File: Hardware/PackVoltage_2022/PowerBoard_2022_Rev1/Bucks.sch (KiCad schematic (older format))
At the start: 80 parts, among them U10 OKI-78SR-12_1.0-W36-C, U11 OKI-78SR-12_1.0-W36-C, U12 OKI-78SR-12_1.0-W36-C, U13 OKI-78SR-12_1.0-W36-C, U14 OKI-78SR-12_1.0-W36-C, U15 OKI-78SR-12_1.0-W36-C, U16 OKI-78SR-12_1.0-W36-C, U17 OKI-78SR-12_1.0-W36-C, U55 OKI-78SR-12_1.0-W36-C, U7 OKI-78SR-5_1.5-W36-C, U8 OKI-78SR-3.3_1.5-W36-C, U9 OKI-78SR-12_1.0-W36-C

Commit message: Actuation shit
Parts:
- added F9: 5A, Fuse:Fuse_0603_1608Metric_Pad1.05x0.95mm_HandSolder, symbol Device:Fuse
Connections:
- net PV: now also F9.2
- net PVLogic renamed PVAct
- new net PVAct2: F9.1
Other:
- moved on the sheet: F1, F4, F5, F6
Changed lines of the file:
@@
 Wire Wire Line
 	6000 3750 6150 3750
-Text HLabel 750  7000 0    50   Input ~ 0
+Text HLabel 750  6750 0    50   Input ~ 0
 PV
 $Comp
 L Device:Fuse F4
 U 1 1 61DCC65E
-P 1300 6700
-F 0 "F4" V 1103 6700 50  0000 C CNN
-F 1 "5A" V 1194 6700 50  0000 C CNN
-F 2 "Fuse:Fuse_0603_1608Metric_Pad1.05x0.95mm_HandSolder" V 1230 6700 50  0001 C CNN
-F 3 "~" H 1300 6700 50  0001 C CNN
-	1    1300 6700
+P 1300 6450
+F 0 "F4" V 1103 6450 50  0000 C CNN
+F 1 "5A" V 1194 6450 50  0000 C CNN
+F 2 "Fuse:Fuse_0603_1608Metric_Pad1.05x0.95mm_HandSolder" V 1230 6450 50  0001 C CNN
+F 3 "~" H 1300 6450 50  0001 C CNN
+	1    1300 6450
 	0    1    1    0
 $EndComp
@@
 L Device:Fuse F6
 U 1 1 61DCD94F
-P 1300 7300
-F 0 "F6" V 1103 7300 50  0000 C CNN
-F 1 "5A" V 1194 7300 50  0000 C CNN
-F 2 "Fuse:Fuse_0603_1608Metric_Pad1.05x0.95mm_HandSolder" V 1230 7300 50  0001 C CNN
-F 3 "~" H 1300 7300 50  0001 C CNN
-	1    1300 7300
-	0    1    1    0
-$EndComp
-Text GLabel 2000 6700 2    50   Input ~ 0
+P 1300 7050
+F 0 "F6" V 1103 7050 50  0000 C CNN
+F 1 "5A" V 1194 7050 50  0000 C CNN
+F 2 "Fuse:Fuse_0603_1608Metric_Pad1.05x0.95mm_HandSolder" V 1230 7050 50  0001 C CNN
+F 3 "~" H 1300 7050 50  0001 C CNN
+	1    1300 7050
+	0    1    1    0
+$EndComp
+Text GLabel 2000 6450 2    50   Input ~ 0
 PV1
-Text GLabel 2000 7300 2    50   Input ~ 0
+Text GLabel 2000 7050 2    50   Input ~ 0
 PV2
 Wire Wire Line
-	1450 6700 2000 6700
-Wire Wire Line
-	1450 7300 2000 7300
-Wire Wire Line
-	1150 6700 850  6700
-Wire Wire Line
-	1150 7300 850  7300
-Wire Wire Line
-	850  6700 850  7000
+	1450 6450 2000 6450
+Wire Wire Line
+	1450 7050 2000 7050
+Wire Wire Line
+	1150 6450 850  6450
+Wire Wire Line
+	1150 7050 850  7050
+Wire Wire Line
+	850  6450 850  6750
 Text GLabel 700  3450 1    50   Input ~ 0
 PV1
@@
 L Device:Fuse F5
 U 1 1 61E23D5F
-P 1300 7000
-F 0 "F5" V 1103 7000 50  0000 C CNN
-F 1 "2A" V 1194 7000 50  0000 C CNN
-F 2 "Fuse:Fuse_0603_1608Metric_Pad1.05x0.95mm_HandSolder" V 1230 7000 50  0001 C CNN
-F 3 "~" H 1300 7000 50  0001 C CNN
-	1    1300 7000
-	0    1    1    0
-$EndComp
-Wire Wire Line
-	1150 7000 850  7000
-Connection ~ 850  7000
-Wire Wire Line
-	850  7000 850  7300
-Wire Wire Line
-	750  7000 850  7000
+P 1300 6750
+F 0 "F5" V 1103 6750 50  0000 C CNN
+F 1 "2A" V 1194 6750 50  0000 C CNN
+F 2 "Fuse:Fuse_0603_1608Metric_Pad1.05x0.95mm_HandSolder" V 1230 6750 50  0001 C CNN
+F 3 "~" H 1300 6750 50  0001 C CNN
+	1    1300 6750
+	0    1    1    0
+$EndComp
+Wire Wire Line
+	1150 6750 850  6750
+Connection ~ 850  6750
+Wire Wire Line
+	850  6750 850  7050
+Wire Wire Line
+	750  6750 850  6750
 $Comp
 L PowerBoard_2022_Rev1-rescue:OKI-78SR-12_1.0-W36-C-Converter_DCDC U10
@@
 Text GLabel 4000 5150 1    50   Input ~ 0
 PV2
-Text GLabel 2000 7000 2    50   Input ~ 0
+Text GLabel 2000 6750 2    50   Input ~ 0
 PVMulti
 Wire Wire Line
-	2000 7000 1450 7000
+	2000 6750 1450 6750
 Wire Wire Line
 	6050 650  6050 1000
@@
 F0 "12VSciLog" 50
 F1 "12VSciLog.sch" 50
-F2 "12VSciLog" O R 9600 5750 50
-F3 "PVLogic" I L 8400 5750 50
+F2 "12VSciAct" O R 9600 5750 50
+F3 "PVAct" I L 8400 5750 50
+F4 "12VGimAct" O R 9600 5850 50
+F5 "PVAct2" I L 8400 5850 50
 $EndSheet
 $Comp
 L Device:Fuse F1
 U 1 1 61E9458E
+P 1300 7350
+F 0 "F1" V 1103 7350 50  0000 C CNN
+F 1 "5A" V 1194 7350 50  0000 C CNN
+F 2 "Fuse:Fuse_0603_1608Metric_Pad1.05x0.95mm_HandSolder" V 1230 7350 50  0001 C CNN
+F 3 "~" H 1300 7350 50  0001 C CNN
+	1    1300 7350
+	0    1    1    0
+$EndComp
+Text GLabel 2000 7350 2    50   Input ~ 0
+PVAct
+Wire Wire Line
+	1450 7350 2000 7350
+Text GLabel 8250 5750 0    50   Input ~ 0
+PVAct
+Wire Wire Line
+	8250 5750 8400 5750
+Text HLabel 9750 5750 2    50   Output ~ 0
+12VSciAct
+Wire Wire Line
+	9600 5750 9750 5750
+Connection ~ 850  7050
+$Comp
+L Device:Fuse F9
+U 1 1 6197848B
 P 1300 7600
-F 0 "F1" V 1103 7600 50  0000 C CNN
+F 0 "F9" V 1103 7600 50  0000 C CNN
 F 1 "5A" V 1194 7600 50  0000 C CNN
 F 2 "Fuse:Fuse_0603_1608Metric_Pad1.05x0.95mm_HandSolder" V 1230 7600 50  0001 C CNN
@@
 $EndComp
 Text GLabel 2000 7600 2    50   Input ~ 0
-PVLogic
+PVAct2
 Wire Wire Line
 	1450 7600 2000 7600
@@
 	1150 7600 850  7600
 Wire Wire Line
-	850  7300 850  7600
-Text GLabel 8250 5750 0    50   Input ~ 0
-PVLogic
-Wire Wire Line
-	8250 5750 8400 5750
-Text HLabel 9750 5750 2    50   Output ~ 0
-12VSciLog
-Wire Wire Line
-	9600 5750 9750 5750
+	850  7050 850  7350
+Wire Wire Line
+	1150 7350 850  7350
+Connection ~ 850  7350
+Wire Wire Line
+	850  7350 850  7600
+Text GLabel 8250 5850 0    50   Input ~ 0
+PVAct2
+Wire Wire Line
+	8250 5850 8400 5850
+Wire Wire Line
+	9600 5850 9750 5850
+Text HLabel 9750 5850 2    50   Output ~ 0
+12VGimAct
 $EndSCHEMATC

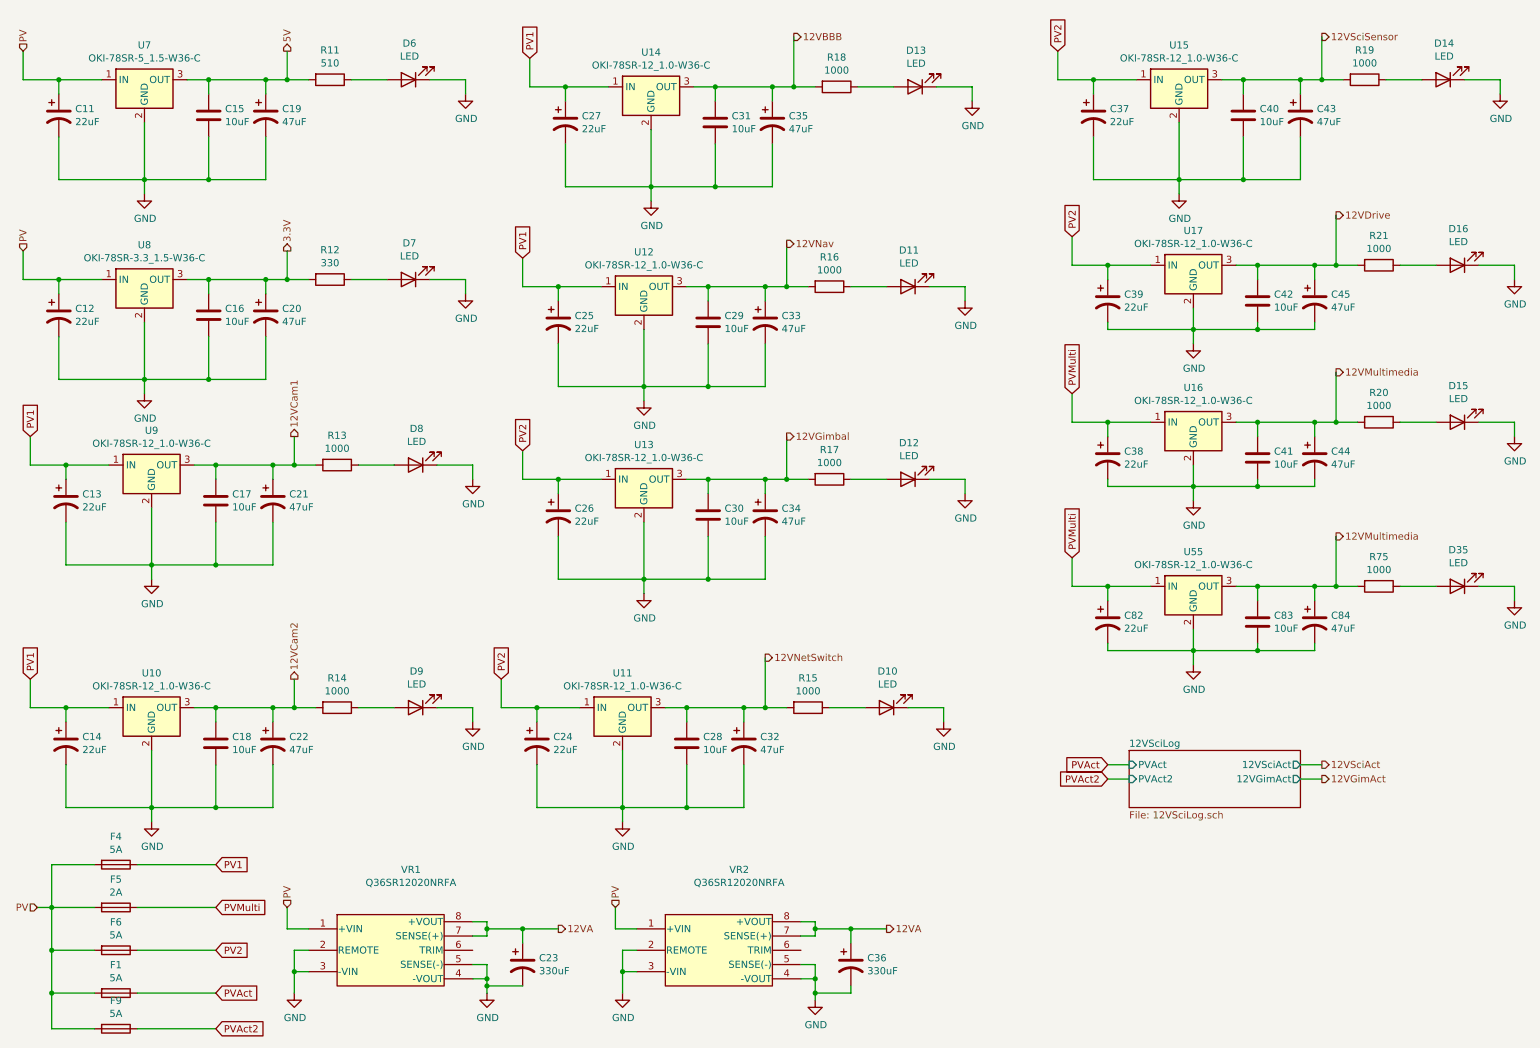
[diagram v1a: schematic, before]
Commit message: Made it to layout, found out about gnd via
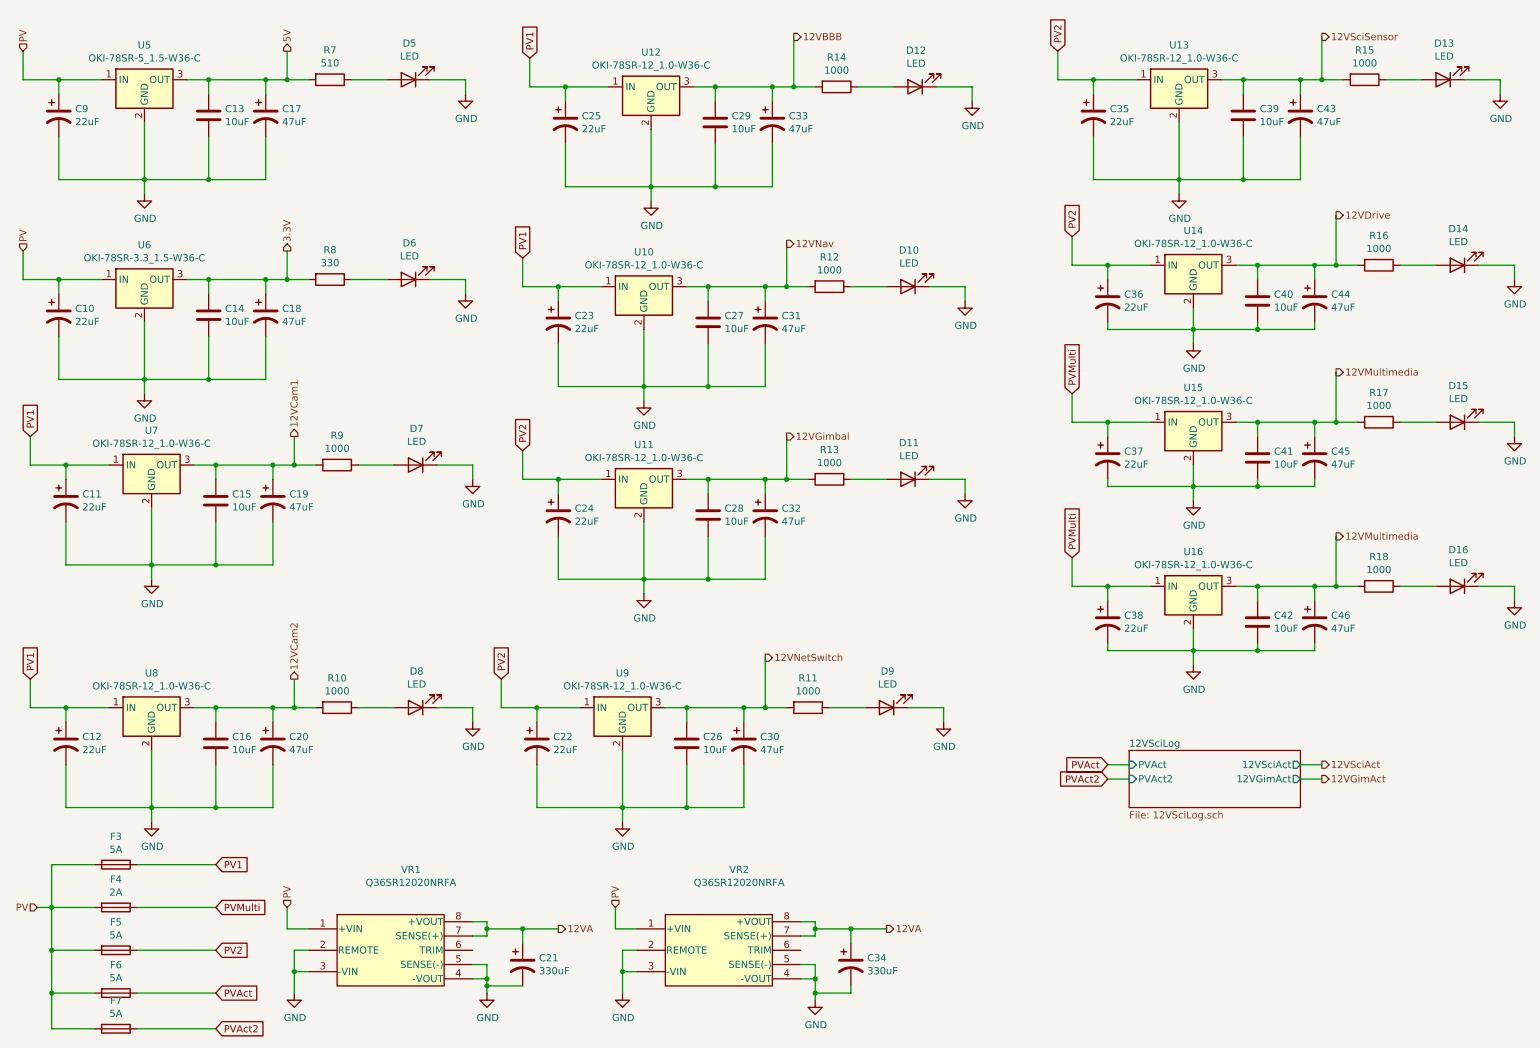
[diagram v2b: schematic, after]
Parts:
- renumbered C12 to C10, C13 to C11, C14 to C12, C15 to C13, C16 to C14, C17 to C15, C18 to C16, C19 to C17, C20 to C18, C21 to C19, C22 to C20, C23 to C21, C24 to C22, C25 to C23, C26 to C24, C27 to C25, C28 to C26, C29 to C27, C30 to C28, C31 to C29, C32 to C30, C33 to C31, C34 to C32, C35 to C33, C36 to C34, C37 to C35, C39 to C36, C38 to C37, C82 to C38, C40 to C39, C42 to C40, C83 to C42, C45 to C44, C44 to C45, C84 to C46, C11 to C9, D11 to D10, D12 to D11, D13 to D12, D14 to D13, D16 to D14, D35 to D16, D6 to D5, D7 to D6, D8 to D7, D9 to D8, D10 to D9, F4 to F3, F5 to F4, F6 to F5, F1 to F6, F9 to F7, R14 to R10, R15 to R11, R16 to R12, R17 to R13, R18 to R14, R19 to R15, R21 to R16, R20 to R17, R75 to R18, R11 to R7, R12 to R8, R13 to R9, U12 to U10, U13 to U11, U14 to U12, U15 to U13, U17 to U14, U16 to U15, U55 to U16, U7 to U5, U8 to U6, U9 to U7, U10 to U8, U11 to U9

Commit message: Organized the parts and changed location of the TIVA
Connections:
- no-connect marks 0 -> 2
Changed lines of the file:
@@
 Text HLabel 9750 5850 2    50   Output ~ 0
 12VGimAct
+NoConn ~ 3800 7050
+NoConn ~ 6100 7050
 $EndSCHEMATC

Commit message: Changed the 2A fuse to a 3A fuse
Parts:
- F4: value 2A -> 3A
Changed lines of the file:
@@
 P 1300 6750
 F 0 "F4" V 1103 6750 50  0000 C CNN
-F 1 "2A" V 1194 6750 50  0000 C CNN
+F 1 "3A" V 1194 6750 50  0000 C CNN
 F 2 "Fuse:Fuse_0603_1608Metric_Pad1.05x0.95mm_HandSolder" V 1230 6750 50  0001 C CNN
 F 3 "~" H 1300 6750 50  0001 C CNN

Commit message: fixed Fuses
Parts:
- F3, F4, F5, F6, F7: footprint Fuse:Fuse_0603_1608Metric_Pad1.05x0.95mm_HandSolder -> MRDT_Passives:ATC_Fuse_Block
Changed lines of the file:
@@
 F 0 "F3" V 1103 6450 50  0000 C CNN
 F 1 "5A" V 1194 6450 50  0000 C CNN
-F 2 "Fuse:Fuse_0603_1608Metric_Pad1.05x0.95mm_HandSolder" V 1230 6450 50  0001 C CNN
+F 2 "MRDT_Passives:ATC_Fuse_Block" V 1230 6450 50  0001 C CNN
 F 3 "~" H 1300 6450 50  0001 C CNN
 	1    1300 6450
@@
 F 0 "F5" V 1103 7050 50  0000 C CNN
 F 1 "5A" V 1194 7050 50  0000 C CNN
-F 2 "Fuse:Fuse_0603_1608Metric_Pad1.05x0.95mm_HandSolder" V 1230 7050 50  0001 C CNN
+F 2 "MRDT_Passives:ATC_Fuse_Block" V 1230 7050 50  0001 C CNN
 F 3 "~" H 1300 7050 50  0001 C CNN
 	1    1300 7050
@@
 F 0 "F4" V 1103 6750 50  0000 C CNN
 F 1 "3A" V 1194 6750 50  0000 C CNN
-F 2 "Fuse:Fuse_0603_1608Metric_Pad1.05x0.95mm_HandSolder" V 1230 6750 50  0001 C CNN
+F 2 "MRDT_Passives:ATC_Fuse_Block" V 1230 6750 50  0001 C CNN
 F 3 "~" H 1300 6750 50  0001 C CNN
 	1    1300 6750
@@
 F 0 "F6" V 1103 7350 50  0000 C CNN
 F 1 "5A" V 1194 7350 50  0000 C CNN
-F 2 "Fuse:Fuse_0603_1608Metric_Pad1.05x0.95mm_HandSolder" V 1230 7350 50  0001 C CNN
+F 2 "MRDT_Passives:ATC_Fuse_Block" V 1230 7350 50  0001 C CNN
 F 3 "~" H 1300 7350 50  0001 C CNN
 	1    1300 7350
@@
 F 0 "F7" V 1103 7600 50  0000 C CNN
 F 1 "5A" V 1194 7600 50  0000 C CNN
-F 2 "Fuse:Fuse_0603_1608Metric_Pad1.05x0.95mm_HandSolder" V 1230 7600 50  0001 C CNN
+F 2 "MRDT_Passives:ATC_Fuse_Block" V 1230 7600 50  0001 C CNN
 F 3 "~" H 1300 7600 50  0001 C CNN
 	1    1300 7600

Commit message: Organized  Stuff into groups and changed how we organize our board
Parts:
- U16: footprint Converter_DCDC:Converter_DCDC_muRata_OKI-78SR_Vertical -> MRDT_Devices:OKI_Horizontal
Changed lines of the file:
@@
 EESchema Schematic File Version 4
-EELAYER 30 0
+LIBS:PowerBoard_2022_Rev1-cache
+EELAYER 26 0
 EELAYER END
 $Descr A4 11693 8268
@@
 F 0 "U16" H 8850 4742 50  0000 C CNN
 F 1 "OKI-78SR-12_1.0-W36-C" H 8850 4651 50  0000 C CNN
-F 2 "Converter_DCDC:Converter_DCDC_muRata_OKI-78SR_Vertical" H 8900 4250 50  0001 L CIN
+F 2 "MRDT_Devices:OKI_Horizontal" H 8900 4250 50  0001 L CIN
 F 3 "https://power.murata.com/data/power/oki-78sr.pdf" H 8850 4500 50  0001 C CNN
 	1    8850 4500
